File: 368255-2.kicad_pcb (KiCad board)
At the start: 2 copper layers, 158 x 114 mm, 27 parts, among them J11 5569-08A2, J2 5569-18A2, J21 Conn_01x01_Pin, J22 Conn_01x01_Pin, J23 Conn_01x01_Pin, J24 Conn_01x01_Pin, J25 Conn_01x01_Pin, J26 Conn_01x01_Pin, J27 Conn_01x01_Pin, J28 Conn_01x01_Pin, J3 5569-06A2, J4 5569-16A2, J5 5569-20A2, P1 368255-2, U1 ULN2003A

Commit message: updated net classes
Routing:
- net GND: track 82.2 -> 4.20 mm
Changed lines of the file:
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@@
 			(size 2.6 2.6)
 			(drill 2.2)
-			(layers "*.Cu" "*.Mask" "F.SilkS")
+			(layers "*.Cu" "*.Mask")
 			(remove_unused_layers no)
 			(net "/OUT_IGN4")
@@
 	)
 	(segment
-		(start 69.97 81.97)
-		(end 83.18119 81.97)
-		(width 1.778)
-		(layer "F.Cu")
-		(net "GND")
-	)
-	(segment
 		(start 83.18119 81.97)
 		(end 83.18119 86.17)
 		(width 1.778)
 		(layer "F.Cu")
-		(net "GND")
-	)
-	(segment
-		(start 46.5 95.5)
-		(end 42.5 95.5)
-		(width 1.778)
-		(layer "F.Cu")
-		(net "GND")
-	)
-	(segment
-		(start 65.45 79)
-		(end 65.45 94.05)
-		(width 1.778)
-		(layer "F.Cu")
-		(net "GND")
-	)
-	(segment
-		(start 65.45 59.24)
-		(end 65.45 79)
-		(width 1.778)
-		(layer "F.Cu")
-		(net "GND")
-	)
-	(segment
-		(start 67 79)
-		(end 69.97 81.97)
-		(width 1.778)
-		(layer "F.Cu")
-		(net "GND")
-	)
-	(segment
-		(start 64 95.5)
-		(end 46.5 95.5)
-		(width 1.778)
-		(layer "F.Cu")
-		(net "GND")
-	)
-	(segment
-		(start 65.45 94.05)
-		(end 64 95.5)
-		(width 1.778)
-		(layer "F.Cu")
-		(net "GND")
-	)
-	(segment
-		(start 42.5 95.5)
-		(end 42 95)
-		(width 1.778)
-		(layer "F.Cu")
-		(net "GND")
-	)
-	(segment
-		(start 65.45 79)
-		(end 67 79)
-		(width 1.778)
-		(layer "F.Cu")

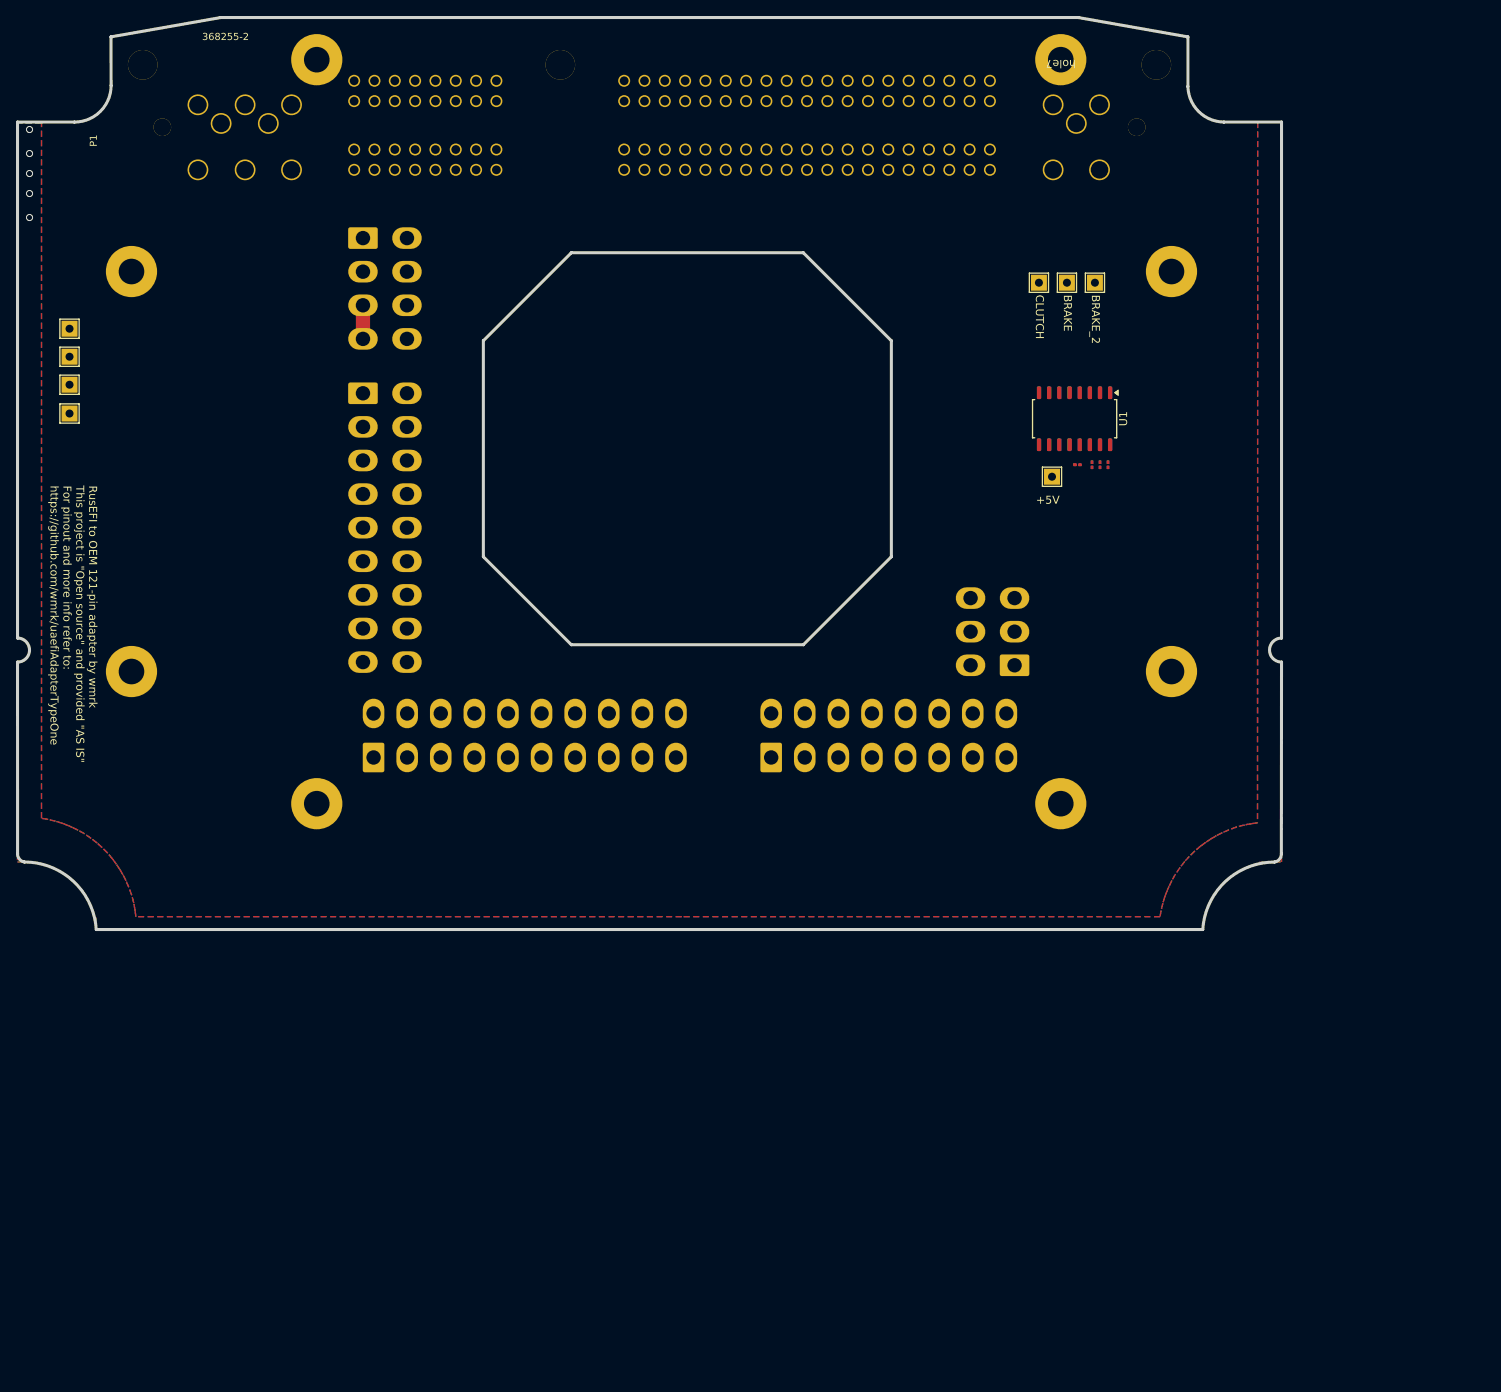
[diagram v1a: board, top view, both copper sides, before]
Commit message: removed unnececary silk+nets+title frame
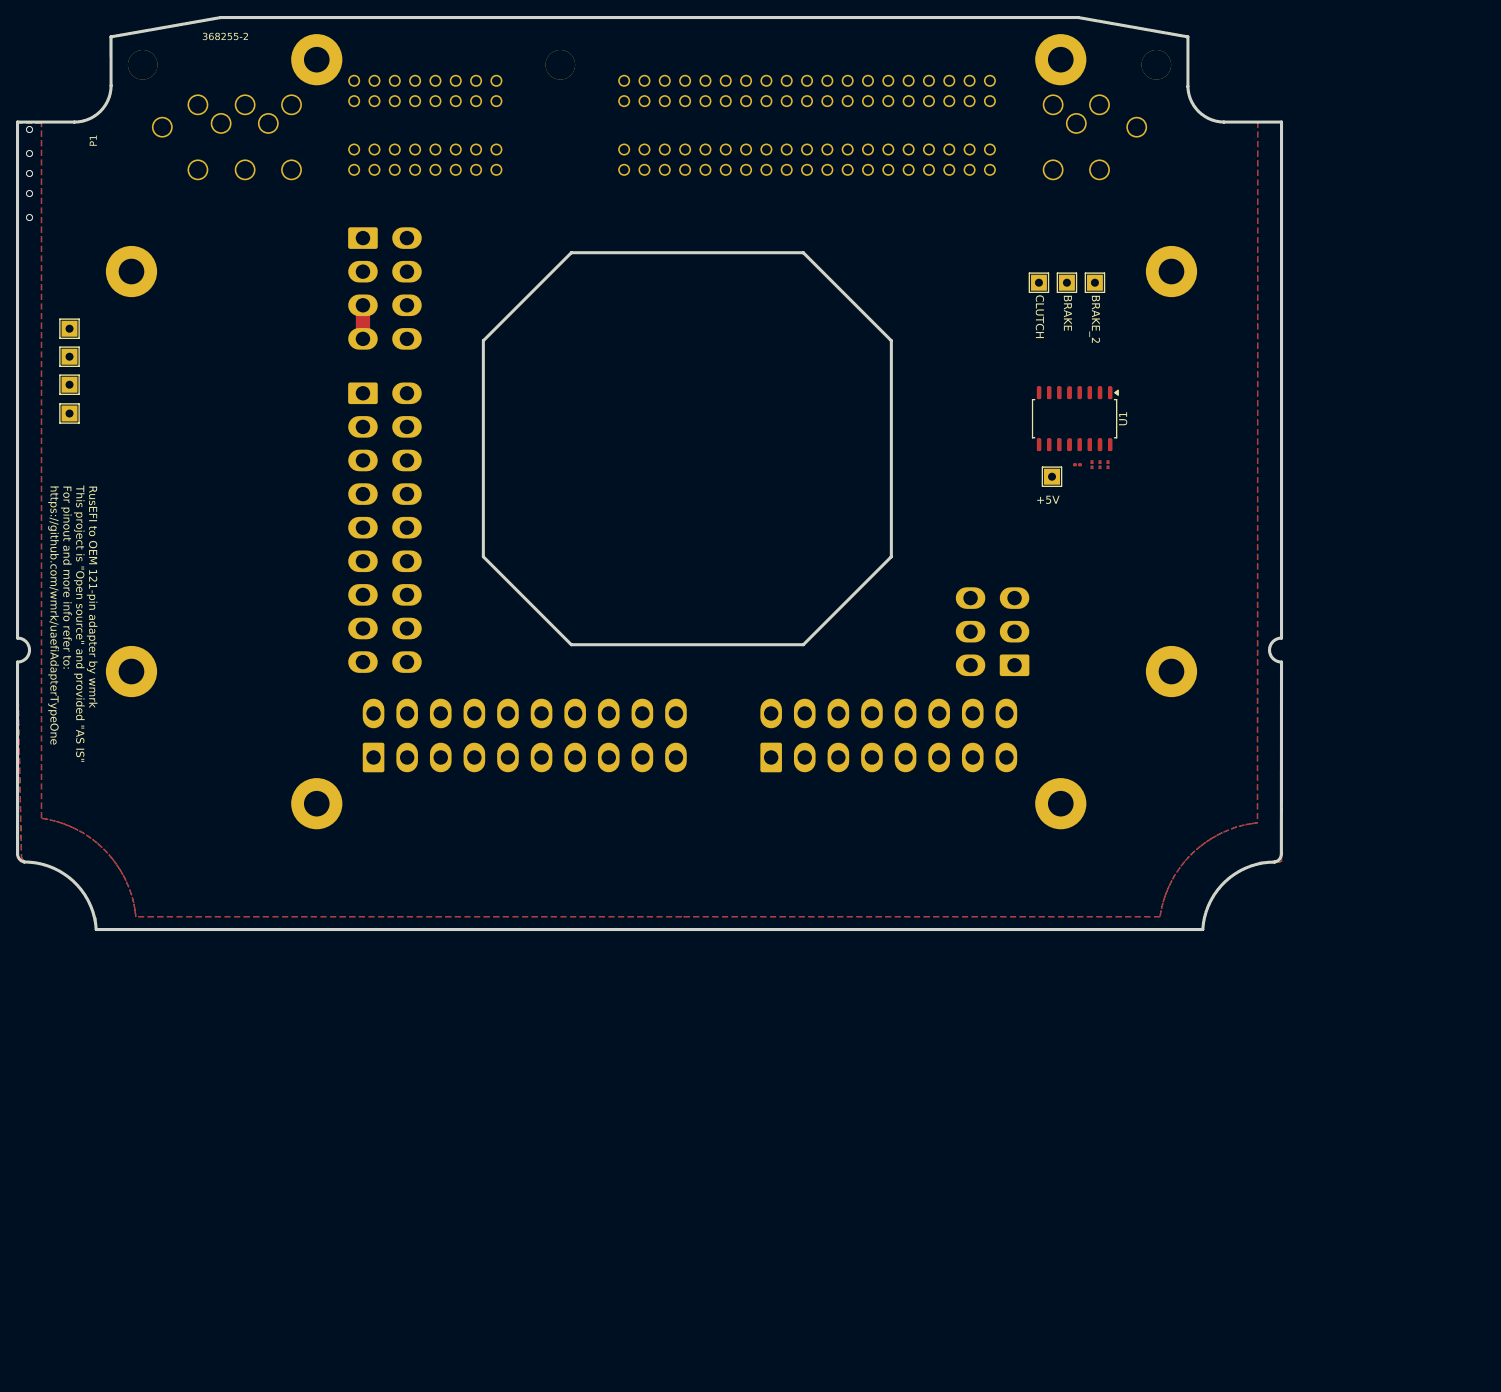
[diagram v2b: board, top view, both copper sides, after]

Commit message: new net classes
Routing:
- net /OUT_DC2+: track 0.00 -> 33.8 mm
- net /OUT_DC2-: track 0.00 -> 32.6 mm
- net GND: vias 5 -> 74

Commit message: tracing but not finished
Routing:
- net +5VP: track 0.00 -> 305.7 mm, vias 0 -> 7
- net GNDA: track 0.00 -> 250.8 mm
- net /OUT_IGN3: track 0.00 -> 246.7 mm, vias 0 -> 4
- net +12V: track 0.00 -> 210.4 mm, vias 0 -> 1
- net GND: track 4.20 -> 209.3 mm, vias 74 -> 75
- net /IN_HALL2: track 0.00 -> 182.9 mm, vias 0 -> 1
- net /IN_PPS2: track 0.00 -> 176.2 mm, vias 0 -> 5
- net /OUT_INJ6: track 0.00 -> 161.9 mm, vias 0 -> 3
- net /3_WBO_Heater: track 0.00 -> 160.0 mm, vias 0 -> 1
- net /6_WBO_Un: track 0.00 -> 158.4 mm, vias 0 -> 2
- net /OUT_INJ3: track 0.00 -> 153.0 mm, vias 0 -> 4
- net /IN_AUX1_EWG_POS_SENSOR: track 0.00 -> 151.4 mm, vias 0 -> 2
- net /OUT_IGN2: track 0.00 -> 151.2 mm, vias 0 -> 1
- net /IN_FLEX: track 0.00 -> 151.0 mm, vias 0 -> 2
- net /OUT_IGN1: track 0.00 -> 144.2 mm, vias 0 -> 1
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
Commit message: refactoring
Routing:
- net /OUT_INJ5: track 71.4 -> 138.0 mm, vias 3 -> 5
- net /OUT_INJ6: track 161.9 -> 134.1 mm
- net /IN_AUX3_FUEL_PRESSURE_SENSOR: track 126.3 -> 109.3 mm
- net /IN_AUX1_EWG_POS_SENSOR: track 151.4 -> 144.8 mm
- net /OUT_DC1-: track 0.00 -> 2.54 mm
- net /VR_MAX9924+: track 125.3 -> 124.0 mm, vias 4 -> 3
- net /OUT_IGN5: track 49.1 -> 50.0 mm
- net +5VP: track 305.7 -> 306.4 mm
- net (no net): vias 0 -> 1
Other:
- outline, holes or cut-outs redrawn

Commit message: tracing has been finished
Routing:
- net /IN_HALL1_SPEED_SENSOR: track 0.00 -> 185.2 mm, vias 0 -> 1
- net /OUT_DC2-: track 118.2 -> 54.3 mm
- net /OUT_DC1+: track 2.54 -> 52.9 mm, vias 0 -> 2
- net /OUT_DC1-: track 2.54 -> 49.3 mm
- net GND: track 209.3 -> 248.4 mm
- net /5_WBO_Rtrim: track 141.3 -> 146.4 mm, vias 5 -> 6
- net +5VP: track 306.4 -> 310.9 mm
- net /IN_HALL3: track 136.7 -> 140.7 mm
- net /IN_HALL2: track 182.9 -> 186.2 mm
- net /IN_AUX1_EWG_POS_SENSOR: track 144.8 -> 147.4 mm
- net /2_WBO_Vm: track 125.3 -> 127.2 mm
- net /OUT_LS3: track 71.9 -> 73.7 mm
- net /IN_AUX3_FUEL_PRESSURE_SENSOR: track 109.3 -> 110.7 mm
- net /3_WBO_Heater: track 160.0 -> 161.2 mm
- net +5VUSB: track 60.8 -> 61.7 mm
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
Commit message: description refinement
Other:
- board text added: "RusEFI to OEM 121-pin adapter by wmrk. This project is Open Source and provided {dblquote}AS IS{dblquote}. For pinout and more info, refer to: https://github.com/wmrk/uaefiAdapterTypeOne"
- board text removed: "RusEFI to OEM 121-pin adapter by wmrk This project is {dblquote}Open source{dblquote} and provided {dblquote}AS IS{dblquote} For pinout and more info refer to: https://github.com/wmrk/uaefiAdapterTypeOne"
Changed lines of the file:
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@@
 		)
 	)
-	(gr_text "RusEFI to OEM 121-pin adapter by wmrk\nThis project is {dblquote}Open source{dblquote} and provided {dblquote}AS IS{dblquote}\nFor pinout and more info refer to:\nhttps://github.com/wmrk/uaefiAdapterTypeOne"
+	(gr_text "RusEFI to OEM 121-pin adapter by wmrk.\nThis project is Open Source and provided {dblquote}AS IS{dblquote}.\nFor pinout and more info, refer to:\nhttps://github.com/wmrk/uaefiAdapterTypeOne"
 		(at 44 104.5 270)
 		(layer "F.SilkS")
